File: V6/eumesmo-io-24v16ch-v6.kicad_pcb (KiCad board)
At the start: 4 copper layers, 128 x 67.8 mm, 343 parts, among them J1 250-208, J2 250-208, J3 250-208, J4 250-208, J5 250-202, J6 250-202, J7 USB_C_Receptacle_USB2.0, J8 ETHERNET, J9 250-203, Q1 WPM2015-3/TR, Q10 MMBT2222A, Q11 MMBT2222A, Q12 MMBT2222A, Q13 MMBT2222A, Q14 MMBT2222A, Q15 MMBT2222A, Q16 MMBT2222A, Q17 MMBT2222A, Q18 MMBT2222A, Q19 MMBT2222A, Q2 MMUN2211LT3G, Q3 UMH3N, Q4 MMBT2222A, Q5 MMBT2222A, Q6 MMBT2222A, Q7 MMBT2222A, Q8 MMBT2222A, Q9 MMBT2222A, SW1 RESET, SW2 1WIRE_SEL, U1 TX4138, U10 MCP23017, U11 DS2482S-100, U12 OR-3H7-4, U13 OR-3H7-4, U14 OR-3H7-4, U15 OR-3H7-4, U2 SY8089A1AAC, U3 TPS3820-33, U4 CH340K, U5 ESP32-WROOM-32UE-N16, U6 LAN8710A, U7 TPS3823-33, U8 MCP23008, U9 MCP23008

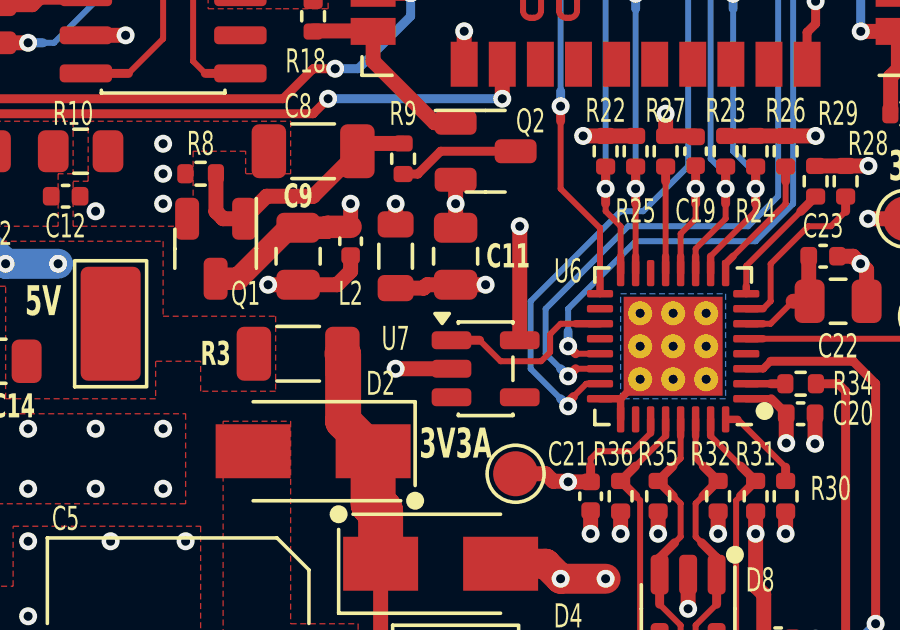
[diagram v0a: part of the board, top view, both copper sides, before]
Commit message: Replaced U7 TPS3823-33 (200ms) for a TPS3820-33 (25ms)
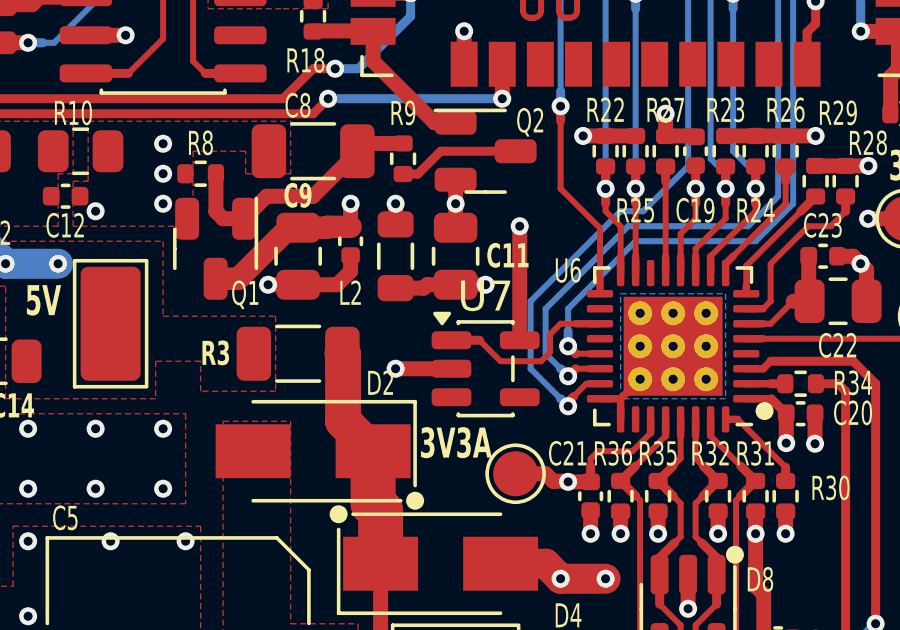
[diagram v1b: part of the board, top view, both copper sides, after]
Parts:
- U7: value TPS3823-33 -> TPS3820-33

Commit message: Added jumper to 1-wire interface
The jumper JP1 must be closed to connect the 1-wire input to GPIO16 when the dip switch and the 1-wire master IC are not installed.
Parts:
- added JP1: 1WJUMPER, Jumper:SolderJumper-2_P1.3mm_Open_RoundedPad1.0x1.5mm, F.Cu at (148.8, 88.3)
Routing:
- net /I2C Devices/1WIREGPIO: track 32.4 -> 35.8 mm
- net /I2C Devices/1WIREBUS: track 13.0 -> 14.1 mm

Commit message: ETH connector repositioned.
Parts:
- removed TP1: TP5019, Tales:TestPoint_Keystone_5019_Miniature
- removed TP13, TP4, TP5: TP, TestPoint:TestPoint_Pad_D1.5mm
- moved D8 2.75 mm to (175.8, 105.1)
- moved J8 2.50 mm to (176.3, 120.1)
- moved R33 2.25 mm to (167.0, 111.1)
- moved C21 1.50 mm to (171.0, 104.1)
- moved R30 1.50 mm to (180.5, 104.1)
- moved R31 1.50 mm to (179.5, 104.1)
- moved R32 1.50 mm to (178.3, 104.1)
- moved R35 1.50 mm to (173.3, 104.1)
- moved R36 1.50 mm to (172.0, 104.1)
- moved C24 1.00 mm to (178.8, 107.8)
- moved C20 0.75 mm to (180.3, 101.3)
- moved R34 0.75 mm to (180.3, 100.3)
- moved D4 0.50 mm to (167.0, 106.3)
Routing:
- net /Power/5VSH: track 13.1 -> 7.53 mm
- net +3V3A: track 48.9 -> 45.6 mm
- net /LAN/ETHLEDGA: track 43.2 -> 40.1 mm
- net /LAN/ETHLEDYK: track 33.1 -> 30.2 mm
- net /LAN/ETHTXD+: track 17.9 -> 16.5 mm
- net /LAN/ETHRXD-: track 15.1 -> 13.7 mm
- net +3V3LAN: track 20.0 -> 18.7 mm, vias 7 -> 6
- net /LAN/RBIAS: track 3.12 -> 4.35 mm
- net /LAN/ETHSH: track 32.8 -> 33.9 mm
- net /LAN/ETHLEDY: track 1.30 -> 2.05 mm
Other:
- board text removed: "3V3A"
- board text removed: "5VSH"
- board text removed: "CLK"
